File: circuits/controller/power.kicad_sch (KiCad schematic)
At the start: 21 parts, among them U7 MIC29302WU, U8 REG_AMS1117-3.3, U9 MIC29302WU

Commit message: sent to fab! 0.6
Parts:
- removed C1: C_10uF, Capacitor_SMD:C_0805_2012Metric_Pad1.18x1.45mm_HandSolder, symbol Open_Automation:C_10uF
- removed C2: C_10uF_Ta, Capacitor_Tantalum_SMD:CP_EIA-6032-15_Kemet-U_Pad2.25x2.35mm_HandSolder, symbol Open_Automation:C_10uF_Ta
- removed D2, D3, D4: LED_G, LED_SMD:LED_0603_1608Metric_Pad1.05x0.95mm_HandSolder, symbol Open_Automation:LED_G
- removed R17, R36: R_10K_0402, Resistor_SMD:R_0402_1005Metric_Pad0.72x0.64mm_HandSolder, symbol Open_Automation:R_10K_0402
- removed R32: R_20K, Resistor_SMD:R_0402_1005Metric_Pad0.72x0.64mm_HandSolder, symbol Open_Automation:R_20K
- removed R33: R_6.8K, Resistor_SMD:R_0603_1608Metric_Pad0.98x0.95mm_HandSolder, symbol Open_Automation:R_6.8K
- removed R35: R_70K, Resistor_SMD:R_0603_1608Metric_Pad0.98x0.95mm_HandSolder, symbol Open_Automation:R_70K
- removed U7: MIC29302WU, Package_TO_SOT_SMD:TO-263-5_TabPin3, symbol Open_Automation:MIC29302WU
- added C33: C_10uF, Capacitor_SMD:C_0805_2012Metric_Pad1.18x1.45mm_HandSolder, symbol Open_Automation:C_10uF
- added C36: 22nF, Capacitor_SMD:C_0402_1005Metric, symbol Open Automation:C_22nF
- added C37: C_22uF, Capacitor_SMD:C_0603_1608Metric_Pad1.08x0.95mm_HandSolder, symbol Open Automation:C_22uF
- added D3, D4: White, LED_SMD:LED_0603_1608Metric_Pad1.05x0.95mm_HandSolder, symbol open_automation:LED-0603-W
- added L7: 10uH, Open_Automation:L_4x4, symbol Open Automation:L_10uH
- added R11: 100K, Resistor_SMD:R_0402_1005Metric_Pad0.72x0.64mm_HandSolder, symbol Open Automation:R_100K_0402
- added R12: 13K, Resistor_SMD:R_0603_1608Metric, symbol Open Automation:R_13K
- added U4: REG_MT2492, Package_TO_SOT_SMD:SOT-23-6_Handsoldering, symbol Open Automation:REG_MT2492
- R11: renamed from R19; value R_10K_0402 -> 10K
- R8: renamed from R18; value R_10K_0402 -> 10K
- renumbered C3 to C5, C4 to C6, C5 to C7, C6 to C8, R39 to R10, R38 to R9, U8 to U3, U9 to U4
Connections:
- net 3V3: now also D3.2 (A)
- net 5V: now also C37.1, L7.2, R11.1
- net GND: now also C33.2, C37.2, R12.2, U4.2 (GND)
- net POWER: now also C33.1, U4.4 (EN), U4.5 (VIN)
- net REG_POWER: now also D4.2 (A)
- net at R11.2: now also D4.1 (K)
- net at R8.2: now also D3.1 (K)
- new net: C36.1, U4.1 (BS)
- new net: C36.2, L7.1, U4.6 (SW)
- new net: R11.2, R12.1, U4.3 (FB)

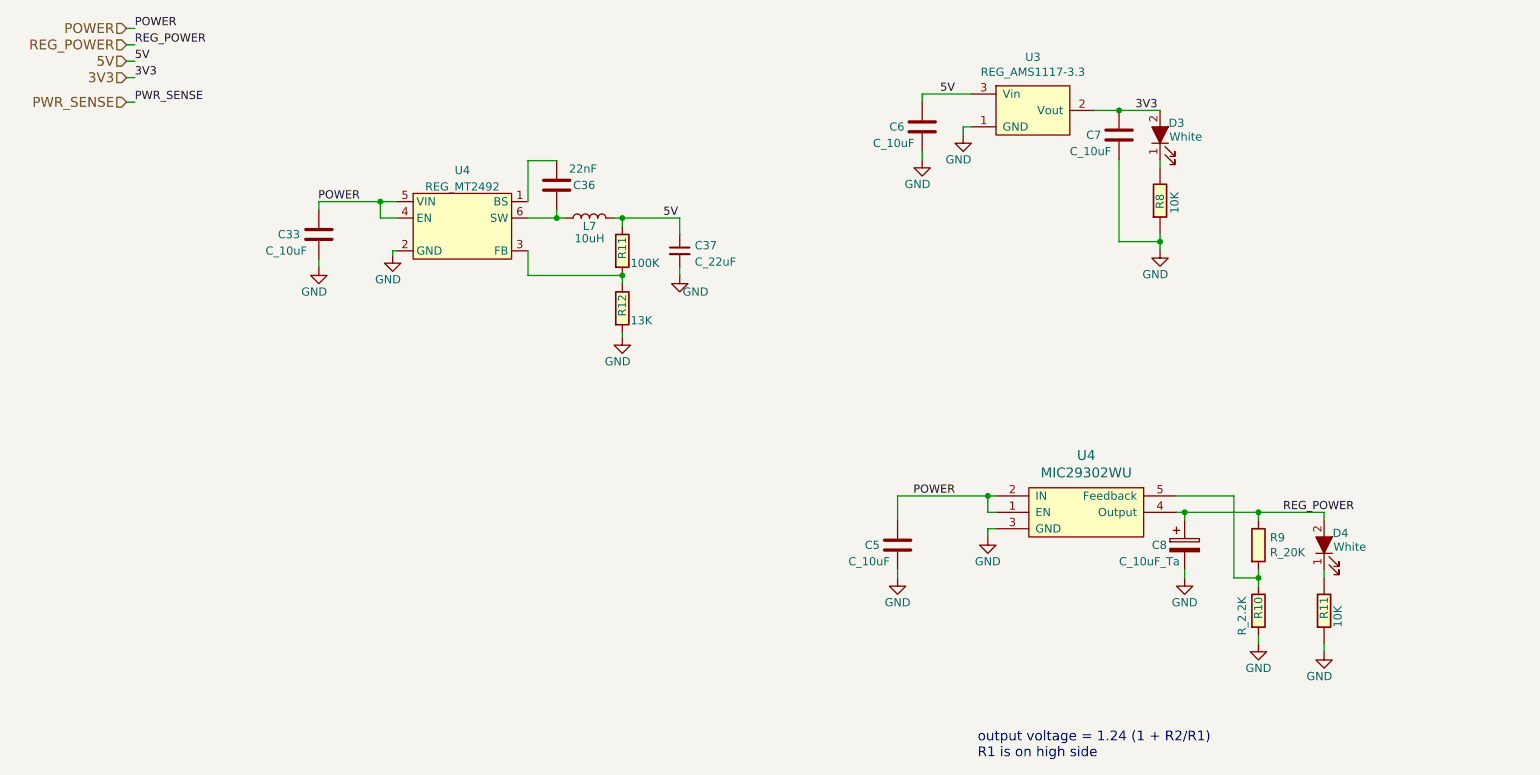
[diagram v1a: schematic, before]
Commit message: powering 5v reg from 12v reg
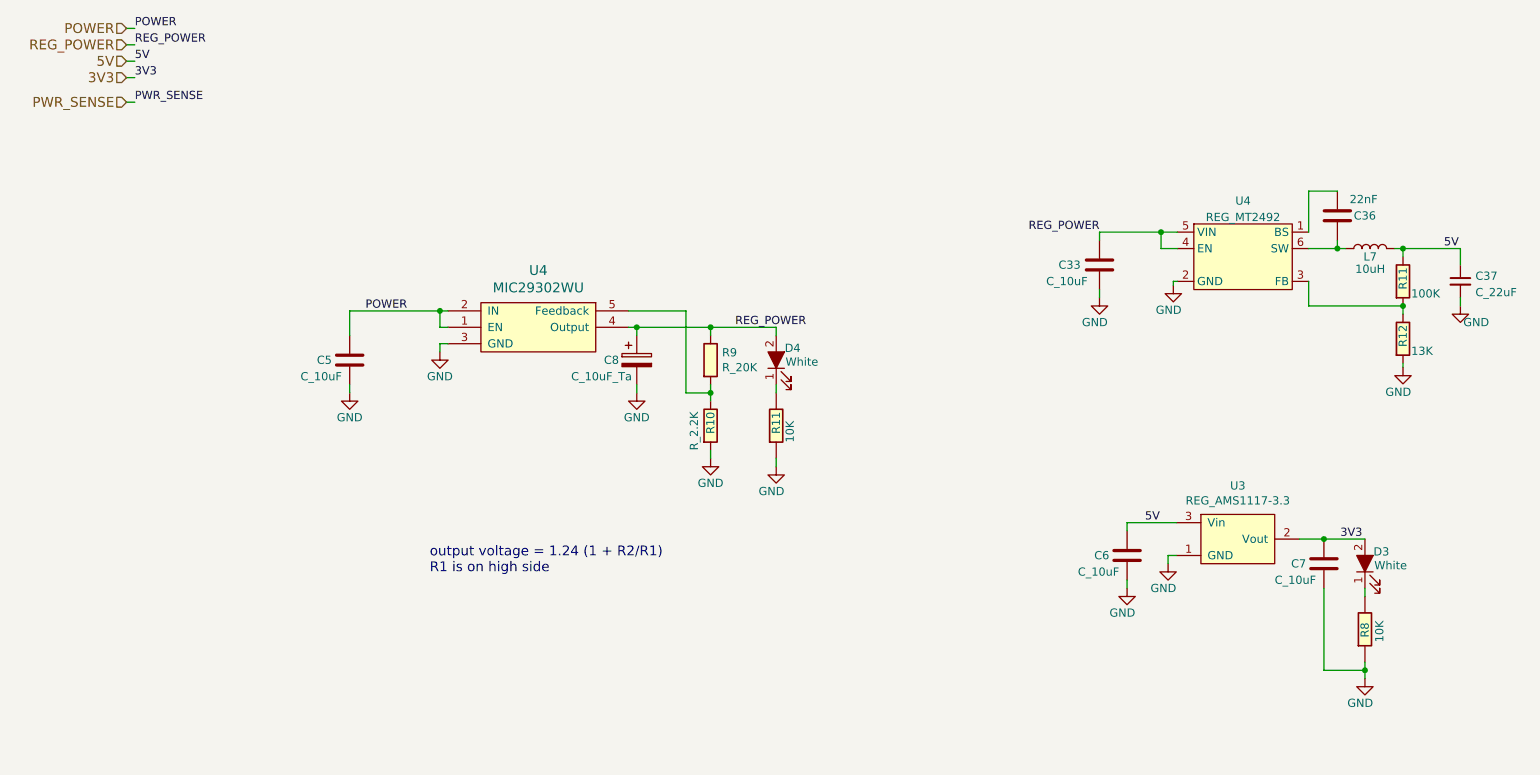
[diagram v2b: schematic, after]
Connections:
- net POWER: no longer C33.1, U4.4 (EN), U4.5 (VIN)
- net REG_POWER: now also C33.1, U4.4 (EN), U4.5 (VIN)
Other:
- moved on the sheet: C33, C36, C37, C5, C6, C7, C8, D3, D4, L7, R10, R11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
